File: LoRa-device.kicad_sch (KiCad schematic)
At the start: 90 parts, among them J1 USB_C_Receptacle_USB2.0_14P, J2 Conn_01x02_Pin, J3 Conn_01x12_Pin, J4 Conn_01x14_Pin, J6 Conn_01x04_Pin, Q1 AO3401A, Q2 S8050, U1 ESP32-S3, U2 W25Q128JVS, U3 MCP73831-2-OT, U4 AMS1117-3.3, U5 Ai-Thinker-Ra-01, U6 BME280, U7 L70-R, Y1 32.768 kHz, Y2 40MHz(10ppm)

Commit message: First routing
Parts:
- removed C1: 100nF, PCM_JLCPCB:C_0402, symbol PCM_JLCPCB-Capacitors:0402,100nF
- removed C5, C9: 15pF, Capacitor_SMD:C_0402_1005Metric, symbol Device:C
- removed U6: BME280, PCM_JLCPCB:Bosch_LGA-8_2.5x2.5mm_P0.65mm_ClockwisePinNumbering, symbol PCM_JLCPCB-Extended:Sensor, BME280
- added DNP4, DNP5: ~, Capacitor_SMD:C_0402_1005Metric, symbol Device:C
- added Q3: AO3401A, Package_TO_SOT_SMD:SOT-23, symbol Transistor_FET:AO3401A
- added R7: 100kΩ, PCM_JLCPCB:R_0402, symbol PCM_JLCPCB-Resistors:0402,100kΩ
- added SW1: SW_Nidec_CAS-120A1, Connector_PinSocket_2.54mm:PinSocket_1x03_P2.54mm_Vertical, symbol Switch:SW_Nidec_CAS-120A1
- DNP2, DNP3: value 15pF -> ~; LCSC C1548 -> (none); MNF PART NUMBER C1548 -> (none)
- U5: LCSC C90040 -> C503593; MNF PART NUMBER C90040 -> C503593
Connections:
- net +3V3: no longer J3.3 (Pin_3)
- net GND: now also J3.3 (Pin_3), DNP4.2, DNP5.2, SW1.1 (C); no longer J3.4 (Pin_4)
- net IO37: now also J3.4 (Pin_4)
- net VSYS: now also Q3.2 (S), R7.2; no longer C7.1, U4.3 (VI)
- net at AE3.1 (FEED), L4.2, R4.2: now also DNP5.1
- net at AE2.1 (FEED), L1.2: now also DNP4.1
- new net: Q3.1 (G), R7.1, SW1.2 (B)
- new net VSYS_SW: C7.1, Q3.3 (D), U4.3 (VI)
- no-connect marks 8 -> 9
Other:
- note removed: "AMBIENT SENSOR"
- moved on the sheet: AE2, AE3, DNP3, L1, L4, R14, R3, R4, R6, U5, U7

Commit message: Completed routing
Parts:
- removed AE2: Antenna, Connector_Coaxial:SMA_Amphenol_132203-12_Horizontal, symbol Device:Antenna_Chip
- removed AE3: Antenna, Connector_Coaxial:U.FL_Molex_MCRF_73412-0110_Vertical, symbol Device:Antenna_Chip
- removed Flash1, Reset1: Tactile Button, 160gf, PCM_JLCPCB:SW_TS-1088-AR02016, symbol PCM_JLCPCB-Connectors_Buttons:Tactile Button, 160gf, 12V, 50mA, 4.0mm
- removed J3: Conn_01x12_Pin, Connector_PinHeader_2.54mm:PinHeader_1x12_P2.54mm_Vertical, symbol Connector:Conn_01x12_Pin
- added FLASH1, RESET1: Tactile Button, 160gf, PCM_JLCPCB:SW_TS-1088-AR02016, symbol PCM_JLCPCB-Connectors_Buttons:Tactile Button, 160gf, 12V, 50mA, 4.0mm
- added J3: Conn_Coaxial, Connector_Coaxial:SMA_Molex_73251-2200_Horizontal, symbol Connector:Conn_Coaxial
- added J5: U.FL, PCM_JLCPCB:IPEX-SMD_BWIPX-1-001E, symbol PCM_JLCPCB-Extended:RF, Connector, U.FL
- added J7: Conn_01x11_Pin, Connector_PinHeader_2.54mm:PinHeader_1x11_P2.54mm_Vertical, symbol Connector:Conn_01x11_Pin
- J2: footprint Connector_PinSocket_2.54mm:PinSocket_1x02_P2.54mm_Vertical -> Connector_PinHeader_2.54mm:PinHeader_1x02_P2.54mm_Vertical
- J4: footprint Connector_PinHeader_2.54mm:PinHeader_1x14_P2.54mm_Vertical -> Connector_PinSocket_2.54mm:PinSocket_1x14_P2.54mm_Vertical
- J6: footprint Connector_PinHeader_2.54mm:PinHeader_1x04_P2.54mm_Vertical -> Connector_PinSocket_2.54mm:PinSocket_1x04_P2.54mm_Vertical
- SW1: footprint Connector_PinSocket_2.54mm:PinSocket_1x03_P2.54mm_Vertical -> Connector_PinHeader_2.54mm:PinHeader_1x03_P2.54mm_Vertical
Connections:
- net +3V3: now also J7.3 (Pin_3)
- net 5V: now also J7.1 (Pin_1)
- net EN: now also RESET1.1 (A)
- net GND: now also FLASH1.2 (B), J3.2 (Ext), J5.2 (Ext), J7.2 (Pin_2), J7.4 (Pin_4), RESET1.2 (B)
- net IO0: now also FLASH1.1 (A)
- net IO12/MISO: now also J7.5 (Pin_5)
- net IO13/MOSI: now also J7.6 (Pin_6)
- net IO14/SCK: now also J7.7 (Pin_7)
- net IO37: now also U5.7 (DIO2)
- net IO38: now also J7.8 (Pin_8)
- net IO39: now also J7.9 (Pin_9)
- net IO41: now also J7.10 (Pin_10)
- net IO42: now also J7.11 (Pin_11)
- net at DNP5.1, L4.2, R4.2: now also J5.1 (In)
- net at DNP4.1, L1.2: now also J3.1 (In)
- no-connect marks 9 -> 8

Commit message: Major rerouting and ESD protection for USB port
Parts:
- removed C36: 10uF, Capacitor_SMD:C_0402_1005Metric, symbol Device:C
- removed L1: 4.7nH, Inductor_SMD:L_0402_1005Metric, symbol Device:L
- added C1: 1uF, Capacitor_SMD:C_0402_1005Metric, symbol Device:C
- added L1: 0R, Resistor_SMD:R_0402_1005Metric, symbol Device:R
- added R10, R11, R13, R31, R8, R9: 10K, Resistor_SMD:R_0402_1005Metric, symbol Device:R
- added R32, R33, R34: 10Ω, PCM_JLCPCB:R_0402, symbol PCM_JLCPCB-Resistors:0402,10Ω
- added U6: USBLC6-2P6, Package_TO_SOT_SMD:SOT-666, symbol Power_Protection:USBLC6-2P6
- DNP1: value 15pF -> ~; LCSC C1548 -> (none); MNF PART NUMBER C1548 -> (none)
- U3: value MCP73831-2-OT -> TP4055; LCSC C7472804 -> C28441; MNF PART NUMBER C7472804 -> TP4055
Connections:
- net +3V3: now also R10.1, R11.1, R13.1, R31.1
- net 5V: now also C1.1, U6.5 (VBUS)
- net GND: now also C1.2, R8.2, R9.2, U6.2 (GND)
- net IO10: now also J4.3 (Pin_3), R10.2
- net IO11: now also J7.9 (Pin_9)
- net IO2: now also U5.7 (DIO2); no longer U7.4 (1PPS)
- net IO33: now also U5.15 (~{NSS}), R13.2; no longer J4.3 (Pin_3)
- net IO35: now also R31.2
- net IO36: now also R11.2
- net IO37: now also U5.6 (DIO1); no longer U5.7 (DIO2)
- net IO40: now also U7.3 (RXD1); no longer U5.15 (~{NSS})
- net IO42: now also U7.2 (TXD1); no longer J7.11 (Pin_11)
- net IO45: now also R8.1
- net IO46: now also R9.1; no longer J4.8 (Pin_8)
- net IO5: now also J7.8 (Pin_8); no longer U5.6 (DIO1)
- net IO6: now also U7.4 (1PPS)
- net IO9: now also J4.8 (Pin_8)
- net RX: now also J7.11 (Pin_11); no longer U7.3 (RXD1)
- net TX: now also J7.10 (Pin_10); no longer U7.2 (TXD1)
- net USB_D+: no longer J1.A6 (D+), J1.B6 (D+), R18.1
- net USB_D-: no longer J1.A7 (D-), J1.B7 (D-), R2.1
- net at DNP2.1, U5.1 (ANT): now also L1.1
- net at DNP4.1, J3.1 (In): now also L1.2
- net IO12/MISO renamed MISOB
- net MISOB: now also R32.2; no longer J6.3 (Pin_3), J7.5 (Pin_5), U5.13 (MISO)
- net IO13/MOSI renamed MOSIB
- net MOSIB: now also R33.2; no longer J6.2 (Pin_2), J7.6 (Pin_6), U5.14 (MOSI)
- net IO14/SCK renamed SCKB
- net SCKB: now also R34.2; no longer J6.4 (Pin_4), J7.7 (Pin_7), U5.12 (SCK)
- net IO3: no longer names the net of U1.8 (GPIO3)
- net IO38 renamed SCKA
- net SCKA: now also J6.4 (Pin_4), U5.12 (SCK); no longer J7.8 (Pin_8)
- net IO39 renamed MOSIA
- net MOSIA: now also J6.2 (Pin_2), U5.14 (MOSI); no longer J7.9 (Pin_9)
- net IO41 renamed MISOA
- net MISOA: now also J6.3 (Pin_3), U5.13 (MISO); no longer J7.10 (Pin_10)
- new net: J1.A6 (D+), J1.B6 (D+), U6.3 (I/O2)
- new net: J1.A7 (D-), J1.B7 (D-), U6.1 (I/O1)
- new net: R18.1, U6.4 (I/O2)
- new net: J7.7 (Pin_7), R34.1
- new net: R2.1, U6.6 (I/O1)
- new net: J7.5 (Pin_5), R32.1
- new net: J7.6 (Pin_6), R33.1
- no-connect marks 8 -> 9
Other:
- moved on the sheet: R18, R2

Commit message: Routing complete, case work begins
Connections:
- net IO10: now also R13.2; no longer R10.2
- net IO33: now also R10.2; no longer R13.2

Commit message: Case work begun, 4 layers board
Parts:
- J3: footprint Connector_Coaxial:SMA_Molex_73251-2200_Horizontal -> Connector_Coaxial:SMA_Molex_73251-1153_EdgeMount_Horizontal
- SW1: footprint Connector_PinHeader_2.54mm:PinHeader_1x03_P2.54mm_Vertical -> Connector_PinHeader_2.54mm:PinHeader_1x02_P2.54mm_Vertical
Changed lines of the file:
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@@
 			)
 		)
-		(property "Footprint" "Connector_Coaxial:SMA_Molex_73251-2200_Horizontal"
+		(property "Footprint" "Connector_Coaxial:SMA_Molex_73251-1153_EdgeMount_Horizontal"
 			(at 111.76 69.85 0)
 			(effects
@@
 			)
 		)
-		(property "Footprint" "Connector_PinHeader_2.54mm:PinHeader_1x03_P2.54mm_Vertical"
+		(property "Footprint" "Connector_PinHeader_2.54mm:PinHeader_1x02_P2.54mm_Vertical"
 			(at 427.99 246.38 0)
 			(effects

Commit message: Further refinements
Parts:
- removed J1: USB_C_Receptacle_USB2.0_14P, Connector_USB:USB_C_Receptacle_HCTL_HC-TYPE-C-16P-01A, symbol Connector:USB_C_Receptacle_USB2.0_14P
- removed J7: Conn_01x11_Pin, Connector_PinHeader_2.54mm:PinHeader_1x11_P2.54mm_Vertical, symbol Connector:Conn_01x11_Pin
- added J1: Connector, USB-TYPE-C-16P, PCM_JLCPCB:TYPE-C-SMD_HX-TYPE-C-16PIN, symbol PCM_JLCPCB-Extended:Connector, USB-TYPE-C-16P
- added J7: Screw_Terminal_01x08, Connector_Phoenix_MC:PhoenixContact_MC_1,5_8-G-3.81_1x08_P3.81mm_Horizontal, symbol Connector:Screw_Terminal_01x08
- added TP1: TestPoint_2Pole, TestPoint:TestPoint_2Pads_Pitch2.54mm_Drill0.8mm, symbol Connector:TestPoint_2Pole
- D4: footprint Diode_SMD:D_SMA -> LED_SMD:LED_0603_1608Metric
- D5: footprint Diode_SMD:D_SOD-123 -> LED_SMD:LED_0603_1608Metric
- R3, R32, R33, R34, R5, R7: footprint PCM_JLCPCB:R_0402 -> Resistor_SMD:R_0402_1005Metric
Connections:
- net +3V3: now also J7.2 (Pin_2)
- net 5V: now also J1.A9B4 (VBUS), J1.B9A4 (VBUS), J7.1 (Pin_1)
- net GND: now also J1.A12B1 (GND), J1.B12A1 (GND), J1.S1 (SHIELD), J7.3 (Pin_3)
- net IO11: now also J7.8 (Pin_8)
- net IO5: now also J7.7 (Pin_7)
- net MISOA: now also R32.2
- net MISOB: no longer R32.2
- net MOSIA: now also R34.2
- net MOSIB: no longer R33.2
- net RX: now also TP1.2
- net SCKA: now also R33.2
- net SCKB: no longer R34.2
- net TX: now also TP1.1
- net at R14.2: now also J1.A5 (CC1)
- net at U6.3 (I/O2): now also J1.A6 (D+), J1.B6 (D+)
- net at U6.1 (I/O1): now also J1.A7 (D-), J1.B7 (D-)
- net at R17.2: now also J1.B5 (CC2)
- net at R34.1: now also J7.6 (Pin_6)
- net at R32.1: now also J7.5 (Pin_5)
- net at R33.1: now also J7.4 (Pin_4)
- no-connect marks 9 -> 11
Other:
- moved on the sheet: R32, R33, R34

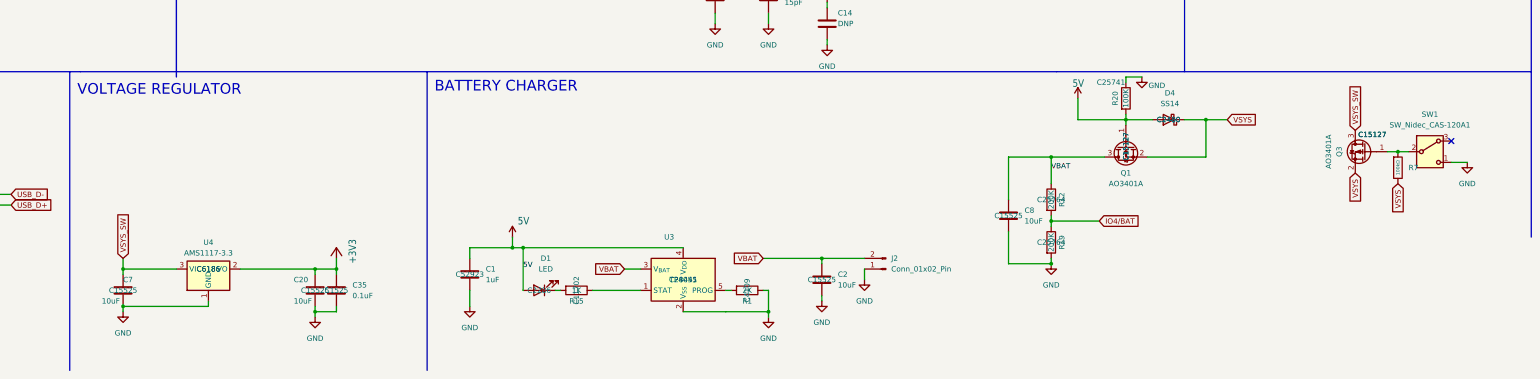
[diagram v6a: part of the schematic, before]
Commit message: Power supply overhaul
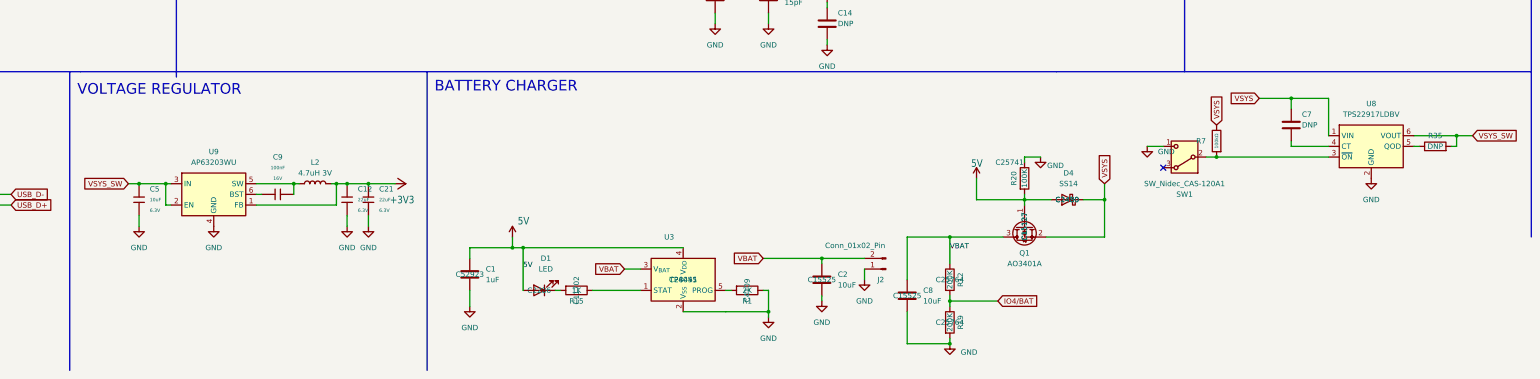
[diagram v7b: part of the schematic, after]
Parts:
- removed C20: 10uF, Capacitor_SMD:C_0402_1005Metric, symbol Device:C
- removed C35: 0.1uF, Capacitor_SMD:C_0402_1005Metric, symbol Device:C
- removed Q3: AO3401A, Package_TO_SOT_SMD:SOT-23, symbol Transistor_FET:AO3401A
- removed U4: AMS1117-3.3, Package_TO_SOT_SMD:SOT-223-3_TabPin2, symbol Regulator_Linear:AMS1117-3.3
- added C12, C21: 22uF, PCM_JLCPCB:C_0603, symbol PCM_JLCPCB-Capacitors:0603,22uF
- added C5: 10uF, PCM_JLCPCB:C_0402, symbol PCM_JLCPCB-Capacitors:0402,10uF
- added C9: 100nF, PCM_JLCPCB:C_0402, symbol PCM_JLCPCB-Capacitors:0402,100nF
- added L2: 4.7uH 3V, Inductor_SMD:L_Sunlord_MWSA0402S, symbol Device:L
- added R35: DNP, Resistor_SMD:R_0402_1005Metric, symbol Device:R
- added U8: TPS22917LDBV, Package_TO_SOT_SMD:SOT-23-6, symbol Power_Management:TPS22917LDBV
- added U9: AP63203WU, Package_TO_SOT_SMD:TSOT-23-6, symbol Regulator_Switching:AP63203WU
- C7: value 10uF -> DNP; LCSC C15525 -> (none); MNF PART NUMBER C15525 -> (none)
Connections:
- net +3V3: now also C12.1, C21.1, L2.2, U9.1 (FB)
- net GND: now also C12.2, C21.2, C5.1, U8.2 (GND), U9.4 (GND); no longer C7.2
- net VSYS: now also C7.1, U8.1 (VIN)
- net VSYS_SW: now also C5.2, R35.2, U8.6 (VOUT), U9.2 (EN), U9.3 (IN); no longer C7.1
- net at R7.1, SW1.2 (B): now also U8.3 (~{ON})
- new net: C7.2, U8.4 (CT)
- new net: R35.1, U8.5 (QOD)
- new net: C9.2, L2.1, U9.5 (SW)
- new net: C9.1, U9.6 (BST)
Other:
- moved on the sheet: C8, D4, Q1, R12, R19, R20, R7, SW1

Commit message: Added secure component
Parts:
- removed C7: DNP, Capacitor_SMD:C_0402_1005Metric, symbol Device:C
- removed DNP3, DNP5: ~, Capacitor_SMD:C_0402_1005Metric, symbol Device:C
- removed J5: U.FL, PCM_JLCPCB:IPEX-SMD_BWIPX-1-001E, symbol PCM_JLCPCB-Extended:RF, Connector, U.FL
- removed L4: DNP, Inductor_SMD:L_0402_1005Metric, symbol Device:L
- removed R3: 0Ω, Resistor_SMD:R_0402_1005Metric, symbol PCM_JLCPCB-Resistors:0402,0Ω
- removed R35: DNP, Resistor_SMD:R_0402_1005Metric, symbol Device:R
- removed R4, R6: 0R, Resistor_SMD:R_0402_1005Metric, symbol Device:R
- removed R8: 10K, Resistor_SMD:R_0402_1005Metric, symbol Device:R
- removed U7: L70-R, RF_GPS:Quectel_L70-R, symbol RF_GPS:L70-R
- added C20, C7: 10uF, PCM_JLCPCB:C_0402, symbol PCM_JLCPCB-Capacitors:0402,10uF
- added C23, C29, C36: 100nF, PCM_JLCPCB:C_0402, symbol PCM_JLCPCB-Capacitors:0402,100nF
- added C24: 33pF, PCM_JLCPCB:C_0402, symbol PCM_JLCPCB-Capacitors:0402,33pF
- added C27, C28: 100pF, PCM_JLCPCB:C_0402, symbol PCM_JLCPCB-Capacitors:0402,100pF
- added C35: 1nF, PCM_JLCPCB:C_0402, symbol PCM_JLCPCB-Capacitors:0402,1nF
- added DNP6, DNP7: ~, Capacitor_SMD:C_0402_1005Metric, symbol Device:C
- added J8: U.FL, PCM_JLCPCB:IPEX-SMD_BWIPX-1-001E, symbol PCM_JLCPCB-Extended:RF, Connector, U.FL
- added L7: DNP, Inductor_SMD:L_0402_1005Metric, symbol Device:L
- added R3, R36: 0R, Resistor_SMD:R_0402_1005Metric, symbol Device:R
- added R8: 0Ω, Resistor_SMD:R_0402_1005Metric, symbol PCM_JLCPCB-Resistors:0402,0Ω
- added U11: L76KB-A58, Lora-device:GPSM-SMD_18P-L10.1-W9.7-P1.10, symbol Lora-device:L76KB-A58
- added U4: ATECC608A-SSHDA, Package_SO:SOIC-8_3.9x4.9mm_P1.27mm, symbol Security:ATECC608A-SSHDA
- R9: value 10K -> 0R; LCSC C25744 -> C17168; MNF PART NUMBER C25744 -> C17168
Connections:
- net +3V3: now also C20.1, C23.1, C24.1, C36.1, C7.1, U11.6 (V_BCKP), U11.8 (VCC), U4.8 (VCC)
- net GND: now also C20.2, C23.2, C24.2, C28.2, C29.2, C36.2, C7.2, DNP6.2, DNP7.2, J8.2 (Ext), R8.2, U11.1 (GND), U11.10 (GND), U11.12 (GND), U4.4 (GND); no longer R9.2
- net IO2: now also U5.5 (DIO0); no longer U5.7 (DIO2)
- net IO37: now also U4.5 (SDA); no longer U5.6 (DIO1)
- net IO40: now also U11.3 (RXD)
- net IO42: now also U11.2 (TXD)
- net IO47: now also U5.6 (DIO1); no longer J4.14 (Pin_14)
- net IO48: now also U4.6 (SCL); no longer U5.5 (DIO0)
- net IO6: now also U11.4 (1PPS)
- net IO7: now also U11.9 (RESET_N)
- net IO8: now also U11.5 (WAKE_UP)
- net VSYS: now also C35.1
- net VSYS_SW: now also R3.2
- net at U8.4 (CT): now also C35.2
- net at U8.5 (QOD): now also R3.1
- net IO45: no longer names the net of U1.51 (GPIO45)
- net IO46: no longer names the net of R9.1
- net IO46: now also DNP6.1, U11.11 (RF_IN); no longer U1.52 (GPIO46)
- new net: C28.1, C29.1, L7.1, R36.1
- new net: C27.2, J8.1 (In), L7.2
- new net: R36.2, U11.14 (VDD_RF)
- new net: R8.1, U11.18 (SET)
- new net: C27.1, DNP7.1, R9.2
- no-connect marks 11 -> 17
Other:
- note added: "SECURE ELEMENT"
- moved on the sheet: DNP2, DNP4, J3, L1, R10, U5
